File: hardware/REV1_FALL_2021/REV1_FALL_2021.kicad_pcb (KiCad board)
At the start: 2 copper layers, 146 x 133.4 mm, 42 parts, among them J101 Screw_Terminal_01x02, J102 Screw_Terminal_01x02, Q101 Q_NMOS_GDS, Q102 Q_NMOS_GDS, U1 Teensy3.6_All_Pins, U2 PA16165_Breakout, U201 TPS2113ADRBR, U3 MPL3115A2_Breakout, U301 TPS2113ADRBR, U4 BNO055_Breakout, U5 RFM69HCW_Breakout

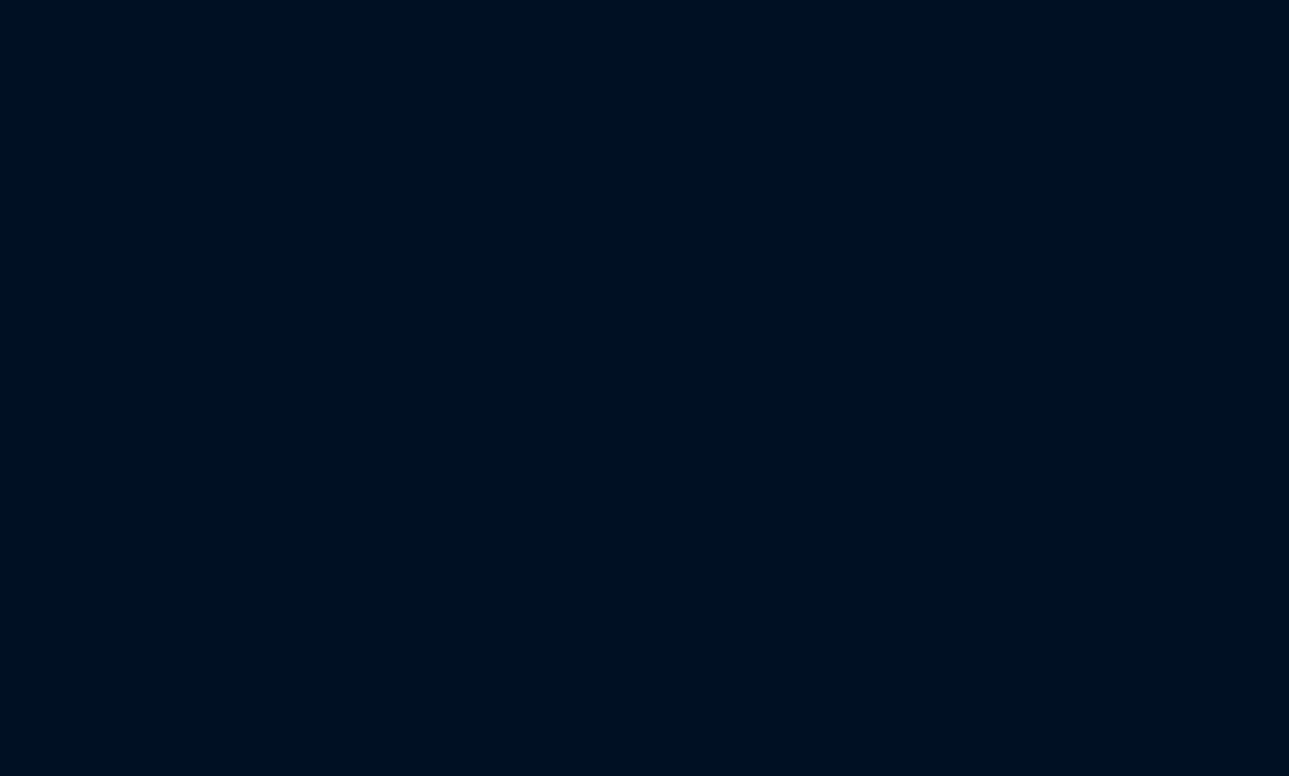
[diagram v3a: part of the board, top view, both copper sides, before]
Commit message: add buzzer to Rev2 schematic and layout
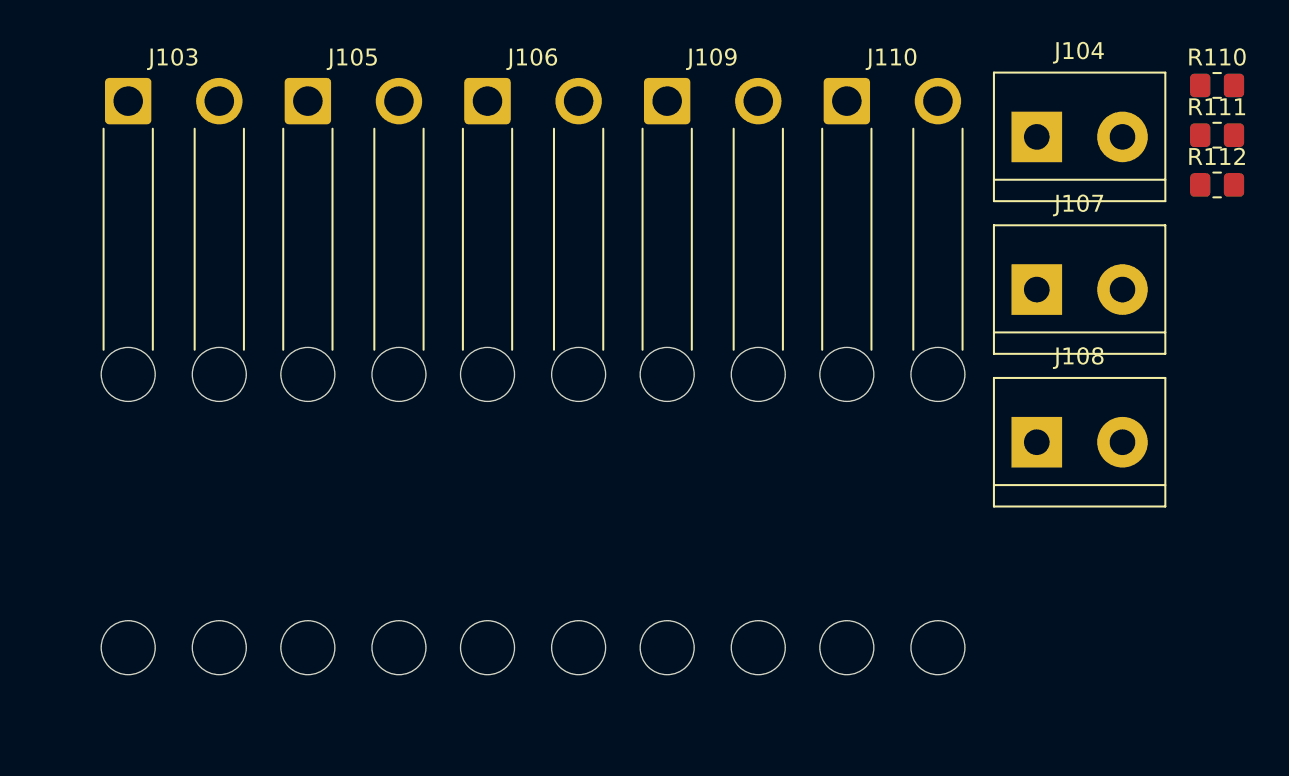
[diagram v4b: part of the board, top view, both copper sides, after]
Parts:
- added J103: Conn_01x02_Female, Connector_Wire:SolderWire-1sqmm_1x02_P5.4mm_D1.4mm_OD2.7mm_Relief2x, F.Cu at (200.1, 24.8)
- added J104: Screw_Terminal_01x02, TerminalBlock:TerminalBlock_bornier-2_P5.08mm, F.Cu at (253.9, 26.9)
- added J105: Conn_01x02_Female, Connector_Wire:SolderWire-1sqmm_1x02_P5.4mm_D1.4mm_OD2.7mm_Relief2x, F.Cu at (210.7, 24.8)
- added J106: Conn_01x02_Female, Connector_Wire:SolderWire-1sqmm_1x02_P5.4mm_D1.4mm_OD2.7mm_Relief2x, F.Cu at (221.4, 24.8)
- added J107: Screw_Terminal_01x02, TerminalBlock:TerminalBlock_bornier-2_P5.08mm, F.Cu at (253.9, 35.9)
- added J108: Screw_Terminal_01x02, TerminalBlock:TerminalBlock_bornier-2_P5.08mm, F.Cu at (253.9, 45.0)
- added J109: Conn_01x02_Female, Connector_Wire:SolderWire-1sqmm_1x02_P5.4mm_D1.4mm_OD2.7mm_Relief2x, F.Cu at (232.0, 24.8)
- added J110: Conn_01x02_Female, Connector_Wire:SolderWire-1sqmm_1x02_P5.4mm_D1.4mm_OD2.7mm_Relief2x, F.Cu at (242.7, 24.8)
- added R110: R_10k, Resistor_SMD:R_0805_2012Metric_Pad1.20x1.40mm_HandSolder, F.Cu at (264.6, 23.8)
- added R111: R_10k, Resistor_SMD:R_0805_2012Metric_Pad1.20x1.40mm_HandSolder, F.Cu at (264.6, 26.8)
- added R112: R_10k, Resistor_SMD:R_0805_2012Metric_Pad1.20x1.40mm_HandSolder, F.Cu at (264.6, 29.7)
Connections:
- C203 pad 1: /V_EMATCH -> /TPS2113A for E-match/VOUT
- C303 pad 1: /V_TEENSY -> /TPS2113A for Teensy power/VOUT
- R101 pad 2: /TPS2113A for Teensy power/VSNS -> /TPS2113A for E-match/VSNS
- R102 pad 1: /TPS2113A for Teensy power/VSNS -> /TPS2113A for E-match/VSNS
- R202 pad 1: /V_EMATCH -> /TPS2113A for E-match/VOUT
- R302 pad 1: /V_TEENSY -> /TPS2113A for Teensy power/VOUT
- U1 pad 34: /BALANCE_CONTROL -> /KEY_SWITCH_DIGITAL
- U201 pad 3: /BALANCE_CONTROL -> /TPS2113A for E-match/VSNS
- U201 pad 7: /V_EMATCH -> /TPS2113A for E-match/VOUT
- U301 pad 3: /TPS2113A for Teensy power/VSNS -> /TPS2113A for E-match/VSNS
- U301 pad 7: /V_TEENSY -> /TPS2113A for Teensy power/VOUT
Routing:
- net /TPS2113A for Teensy power/VSNS: track 7.49 -> 0.00 mm
- net /TPS2113A for E-match/VSNS: track 0.00 -> 7.49 mm
